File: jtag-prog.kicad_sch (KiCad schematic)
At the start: 31 parts, among them J1 USB_C_Receptacle_USB2.0_14P, SW1 BOOT, SW5 BOOT, U10 RP2040, U1001 XC6206PxxxMR, U2 W25Q128JVS, Y1 12Mhz

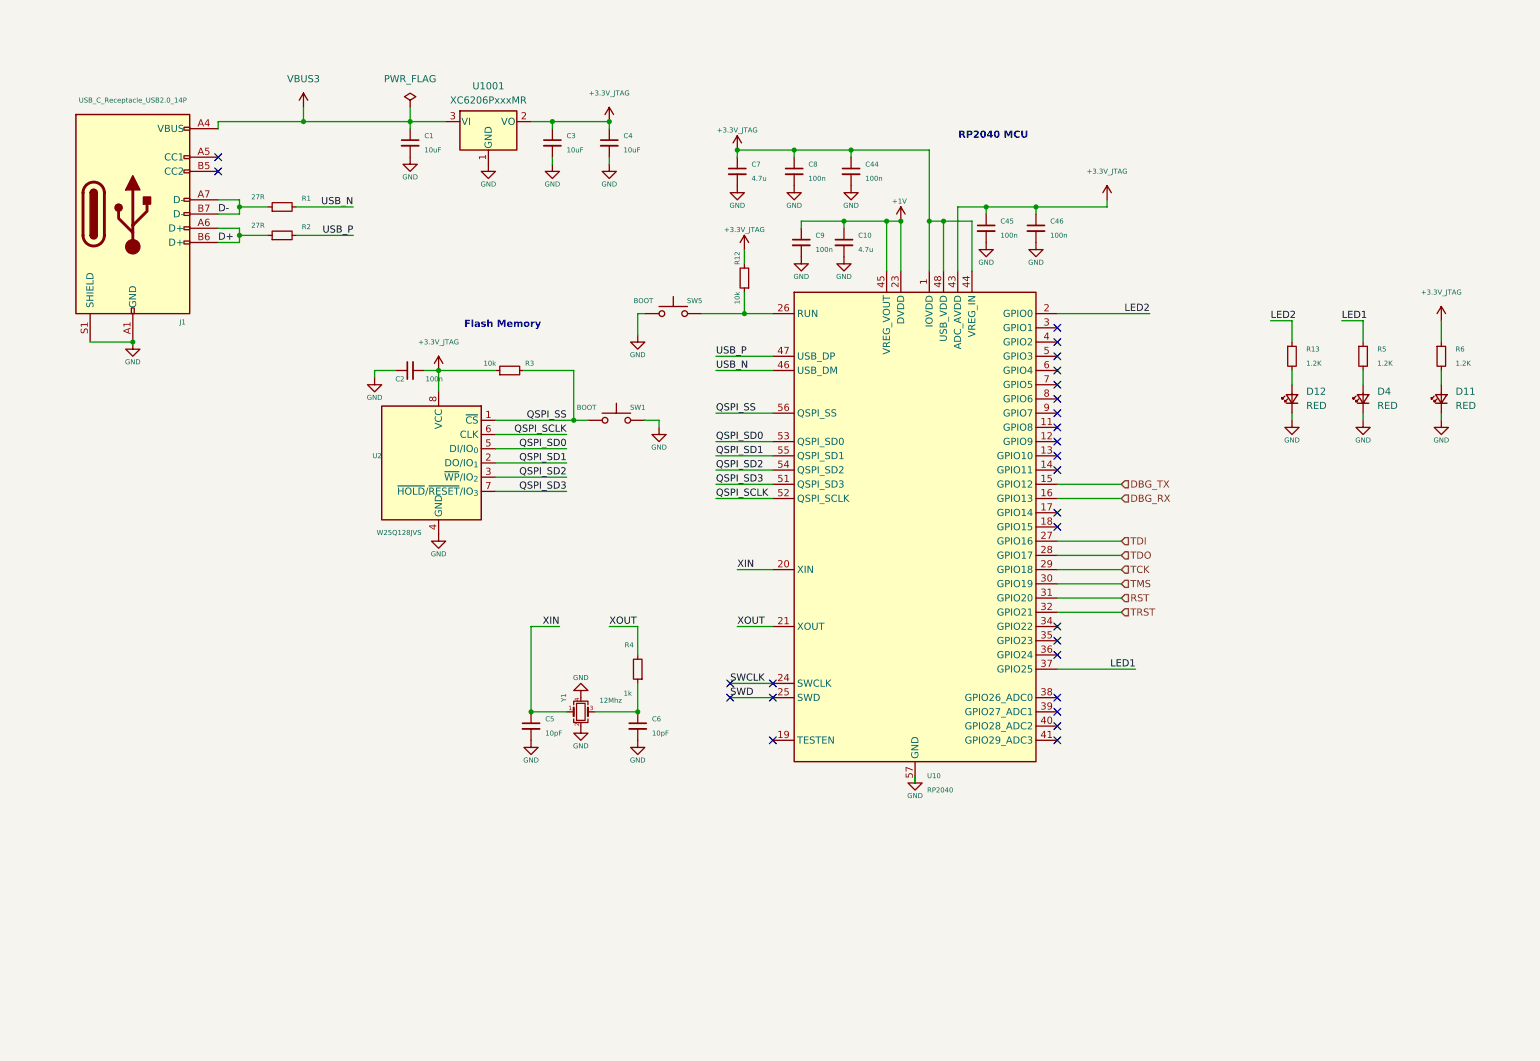
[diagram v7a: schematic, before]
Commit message: Update the BOM and the routing
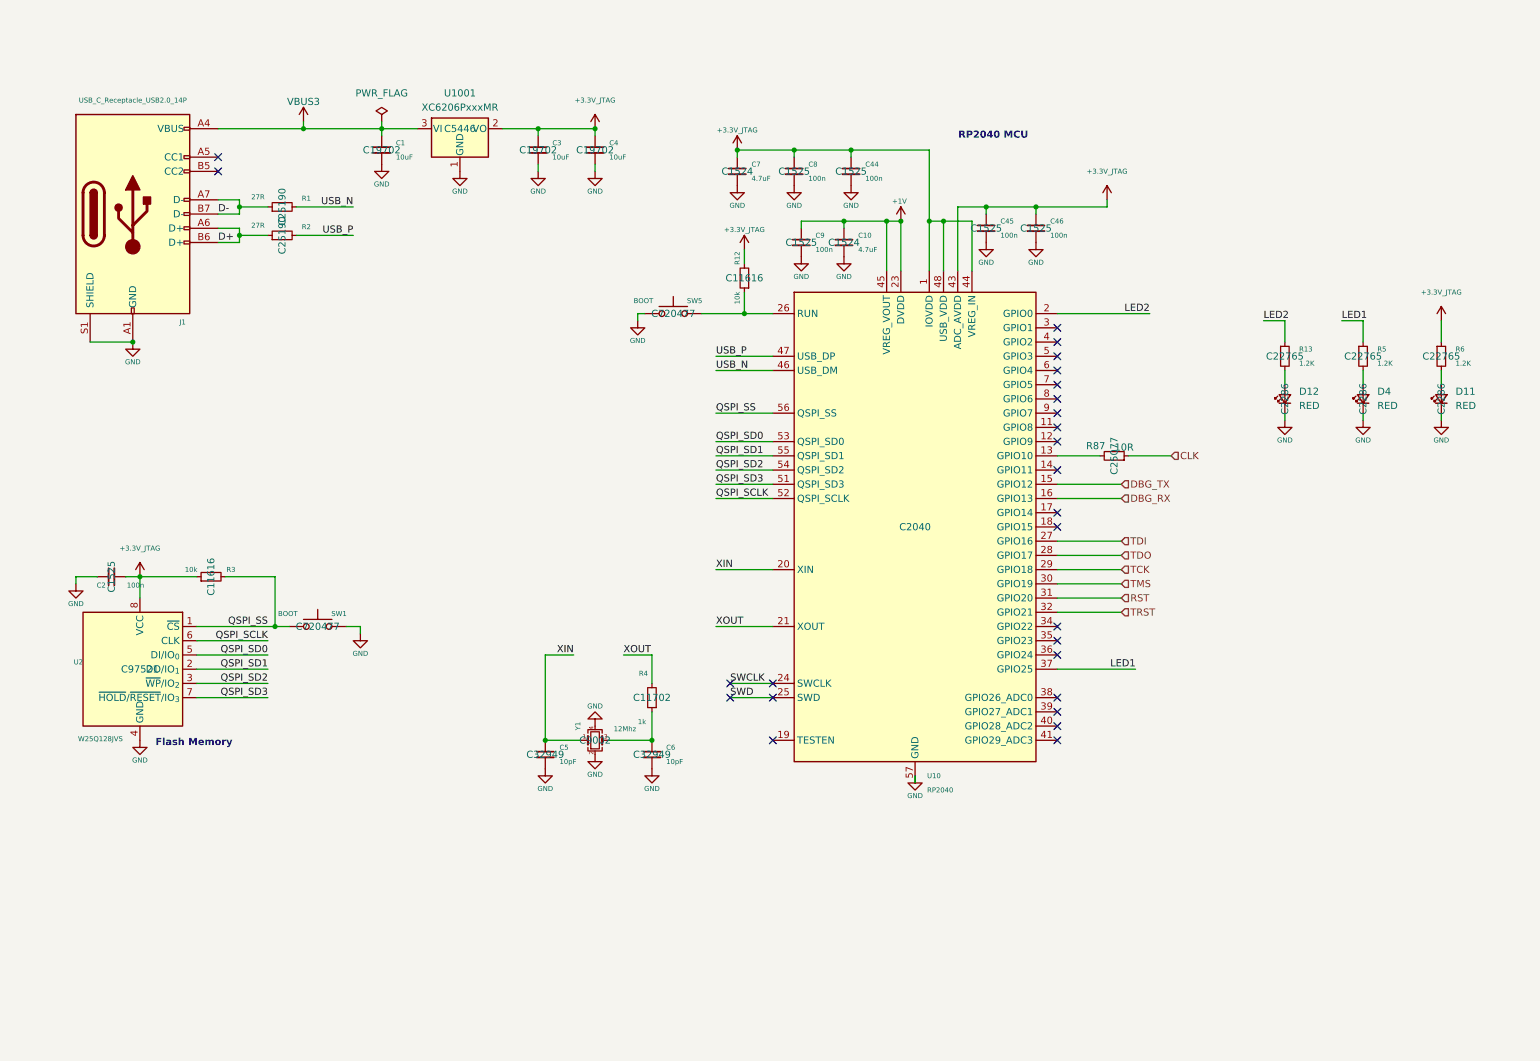
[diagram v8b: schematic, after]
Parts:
- added R87: 10R, Resistor_SMD:R_0402_1005Metric, symbol Device:R_Small
- C1, C3, C4: LCSC (none) -> C19702
- C10, C7: value 4.7u -> 4.7uF; LCSC (none) -> C1524
- C2, C44, C45, C46, C8, C9: LCSC (none) -> C1525
- C5, C6: LCSC (none) -> C32949
- D11, D12, D4: LCSC (none) -> C2286
- R1, R2: footprint Resistor_SMD:R_0402_1005Metric -> Resistor_SMD:R_0603_1608Metric; LCSC (none) -> C25190
- R12, R3: LCSC (none) -> C11616
- R13, R5, R6: footprint Resistor_SMD:R_0402_1005Metric -> Resistor_SMD:R_0603_1608Metric; LCSC (none) -> C22765
- R4: LCSC (none) -> C11702
- SW1, SW5: LCSC (none) -> C720477
- U10: LCSC (none) -> C2040
- U1001: LCSC (none) -> C5446
- U2: LCSC (none) -> C97521
- Y1: LCSC (none) -> C9002
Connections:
- net at U10.13 (GPIO10): now also R87.2
- new net CLK: R87.1
- no-connect marks 27 -> 26
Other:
- moved on the sheet: C1, C2, C3, C4, C5, C6, D12, R13, R3, R4, SW1, U1001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
